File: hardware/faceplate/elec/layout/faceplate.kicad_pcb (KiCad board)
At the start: 2 copper layers, 182.9 x 128.5 mm, 65 parts

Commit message: wip
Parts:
- moved ENC64 7.00 mm to (12.6, 83.4)
- moved ENC65 7.00 mm to (107.3, 83.4)
- moved J10 7.00 mm to (170.6, 50.0)
- moved J11 7.00 mm to (128.6, 64.0)
- moved J12 7.00 mm to (142.6, 64.0)
- moved J13 7.00 mm to (156.6, 64.0)
- moved J14 7.00 mm to (170.6, 64.0)
- moved J15 7.00 mm to (128.6, 76.4)
- moved J16 7.00 mm to (142.6, 76.4)
- moved J17 7.00 mm to (156.6, 76.4)
- moved J18 7.00 mm to (170.6, 76.4)
- moved J19 7.00 mm to (128.6, 88.8)
- moved J20 7.00 mm to (142.6, 88.8)
- moved J21 7.00 mm to (156.6, 88.8)
- moved J22 7.00 mm to (170.6, 88.8)
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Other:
- board size 182.9 x 128.5 mm -> 181.9 x 127.5 mm

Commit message: Routed
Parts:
- moved J23 8.52 mm to (124.0, 94.0)
- moved J19 8.18 mm to (124.0, 82.0)
- moved J24 8.03 mm to (139.0, 94.0)
- moved J15 7.85 mm to (124.0, 70.0)
- moved J20 7.67 mm to (139.0, 82.0)
- moved J25 7.64 mm to (154.0, 94.0)
- moved J11 7.53 mm to (124.0, 58.0)
- moved J26 7.36 mm to (169.0, 94.0)
- moved J16 7.32 mm to (139.0, 70.0)
- moved J21 7.26 mm to (154.0, 82.0)
- moved J27 7.22 mm to (124.0, 108.0)
- moved J22 6.97 mm to (169.0, 82.0)
- moved J12 6.97 mm to (139.0, 58.0)
- moved J17 6.89 mm to (154.0, 70.0)
- moved J28 6.63 mm to (139.0, 108.0)
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
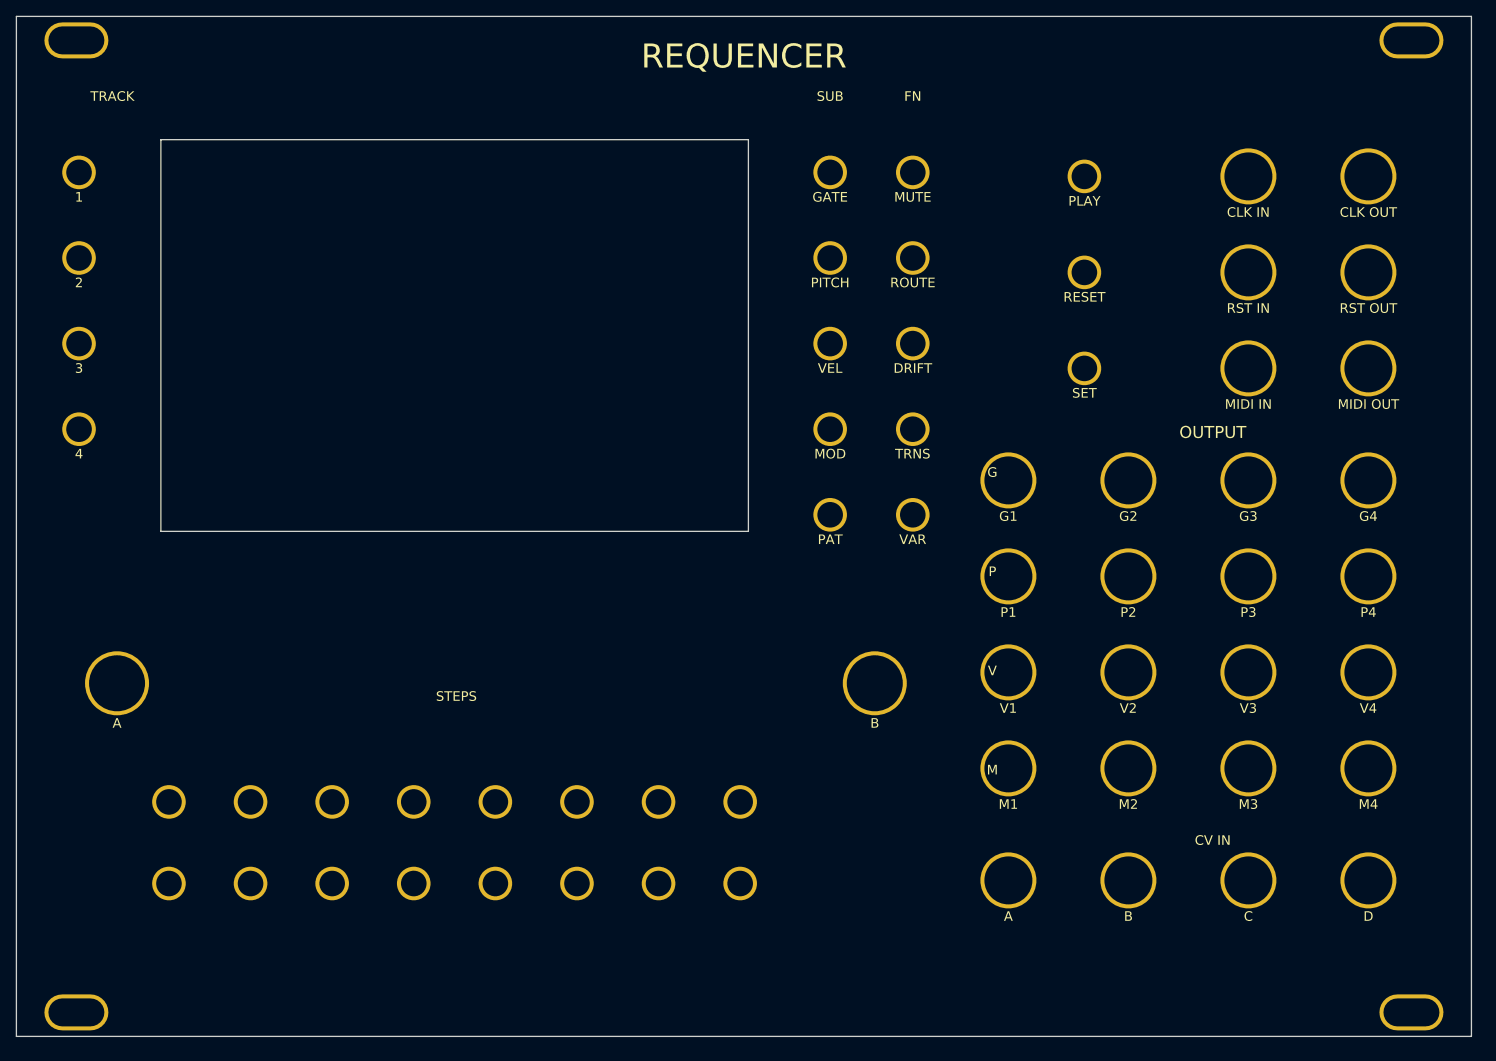
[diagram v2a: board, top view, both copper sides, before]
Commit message: Fix hardware pipeline: SD card position, faceplate holes, 3D assembly stack-up
- Fix SD card slot placement below PLAY button with component-map fallback
- Rebuild PJS008U 3D model as hollow card cage, align with faceplate cutout
- Inset USB-C connector flush with main board edge
- Add clock jack holes, SD cutout, JetBrains Mono fonts to faceplate
- Correct 3D assembly Z spacing from actual PJ398SM model measurements
- Improve explode animation: anchor control board, smoother slider
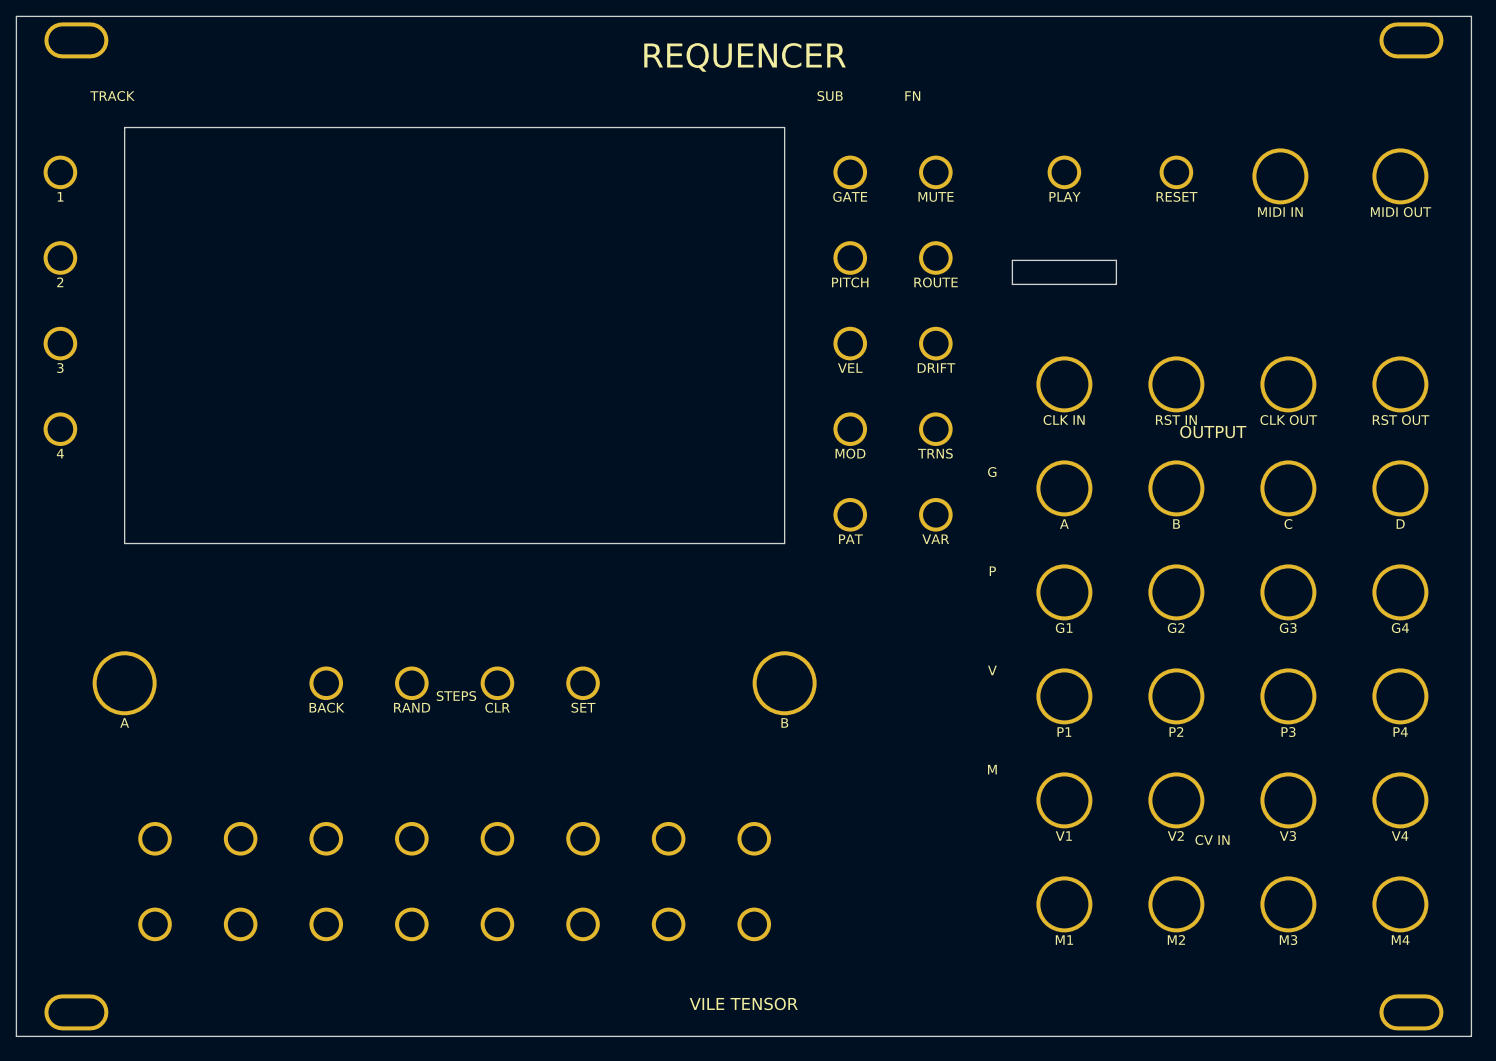
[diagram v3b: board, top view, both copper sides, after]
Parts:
- removed ENC64: , Faceplate:ENC64
- removed ENC65: , Faceplate:ENC65
- added ENC67: , Faceplate:ENC67, F.Cu at (13.5, 83.4)
- added ENC68: , Faceplate:ENC68, F.Cu at (96.0, 83.4)
- added SW64: , Faceplate:SW64, F.Cu at (49.4, 83.4)
- added SW65: , Faceplate:SW65, F.Cu at (60.1, 83.4)
- added SW66: , Faceplate:SW66, F.Cu at (104.2, 62.3)
- moved SW62 74.0 mm to (70.8, 83.4)
- moved SW63 66.4 mm to (38.7, 83.4)
- moved J27 49.5 mm to (131.0, 59.0)
- moved J28 49.4 mm to (145.0, 59.0)
- moved J29 49.3 mm to (159.0, 59.0)
- moved J30 49.2 mm to (173.0, 59.0)
- moved J7 26.9 mm to (131.0, 46.0)
- moved J23 18.4 mm to (131.0, 111.0)
- moved J24 18.0 mm to (145.0, 111.0)
- moved J25 17.7 mm to (159.0, 111.0)
- moved J19 17.5 mm to (131.0, 98.0)
- moved J26 17.5 mm to (173.0, 111.0)
- moved J8 17.2 mm to (159.0, 46.0)
- moved J20 17.1 mm to (145.0, 98.0)
- moved SW61 17.0 mm to (145.0, 19.5)
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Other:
- outline, holes or cut-outs redrawn
- board text added: "VILE TENSOR"

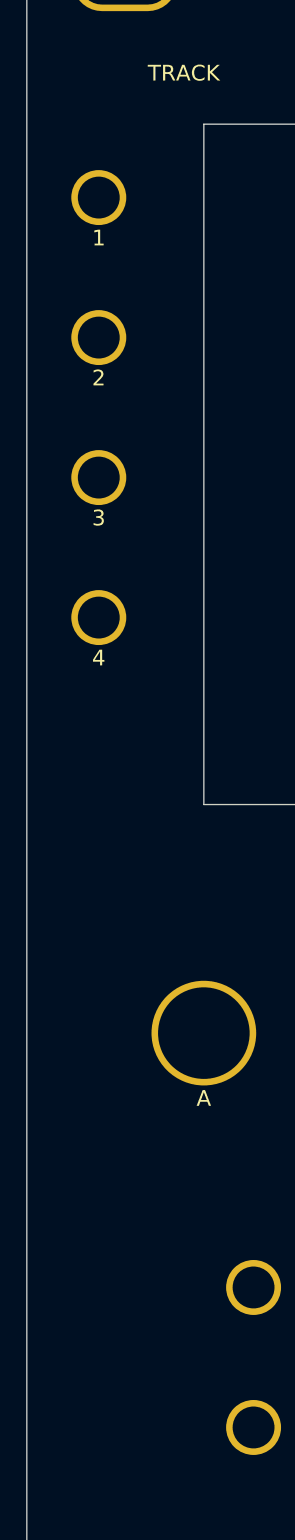
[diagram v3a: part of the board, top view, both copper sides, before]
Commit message: Throughhole m3 for stability
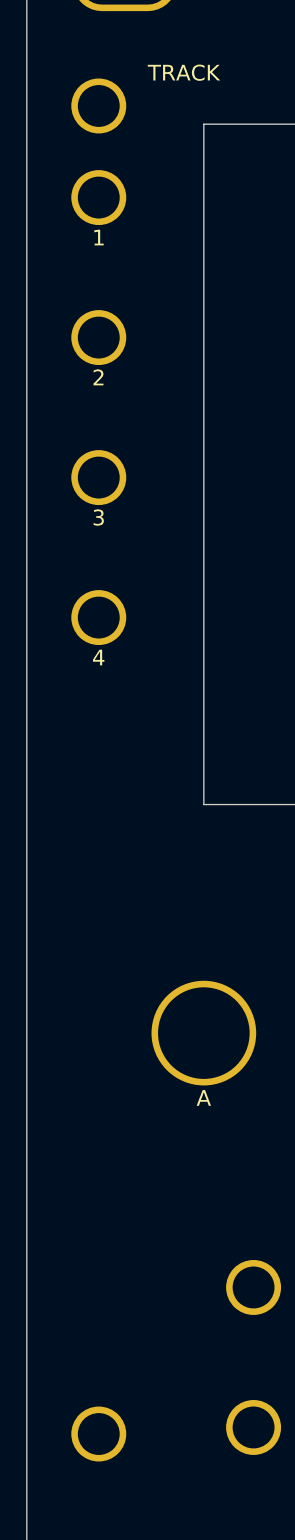
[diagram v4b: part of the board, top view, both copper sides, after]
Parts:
- removed ENC67: , Faceplate:ENC67
- removed ENC68: , Faceplate:ENC68
- removed J5: , Faceplate:J5
- removed J6: , Faceplate:J6
- removed SW31: , Faceplate:SW31
- removed SW32: , Faceplate:SW32
- added ENC69: , Faceplate:ENC69, F.Cu at (13.5, 83.4)
- added ENC70: , Faceplate:ENC70, F.Cu at (96.0, 83.4)
- added J31: , Faceplate:J31, F.Cu at (159.0, 59.0)
- added J32: , Faceplate:J32, F.Cu at (173.0, 59.0)
- added SO5: , Faceplate:SO5, F.Cu at (5.50, 12.5)
- added SO6: , Faceplate:SO6, F.Cu at (5.50, 114.0)
- added SW67: , Faceplate:SW67, F.Cu at (60.1, 83.4)
- added SW68: , Faceplate:SW68, F.Cu at (104.2, 62.3)
- moved SW63 124.0 mm to (145.0, 19.5)
- moved SW44 110.2 mm to (114.9, 51.6)
- moved SW61 107.8 mm to (92.2, 113.5)
- moved SW60 106.2 mm to (81.5, 113.5)
- moved SW35 101.0 mm to (5.50, 40.9)
- moved SW36 101.0 mm to (5.50, 51.6)
- moved SW45 95.9 mm to (114.9, 62.3)
- moved SW62 87.7 mm to (131.0, 19.5)
- moved SW52 65.1 mm to (81.5, 102.8)
- moved SW53 65.1 mm to (92.2, 102.8)
- moved J27 59.1 mm to (159.0, 111.0)
- moved J28 59.1 mm to (173.0, 111.0)
- moved SW66 58.7 mm to (49.4, 83.4)
- moved J12 38.2 mm to (173.0, 46.0)
- moved J7 37.5 mm to (158.0, 20.0)
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
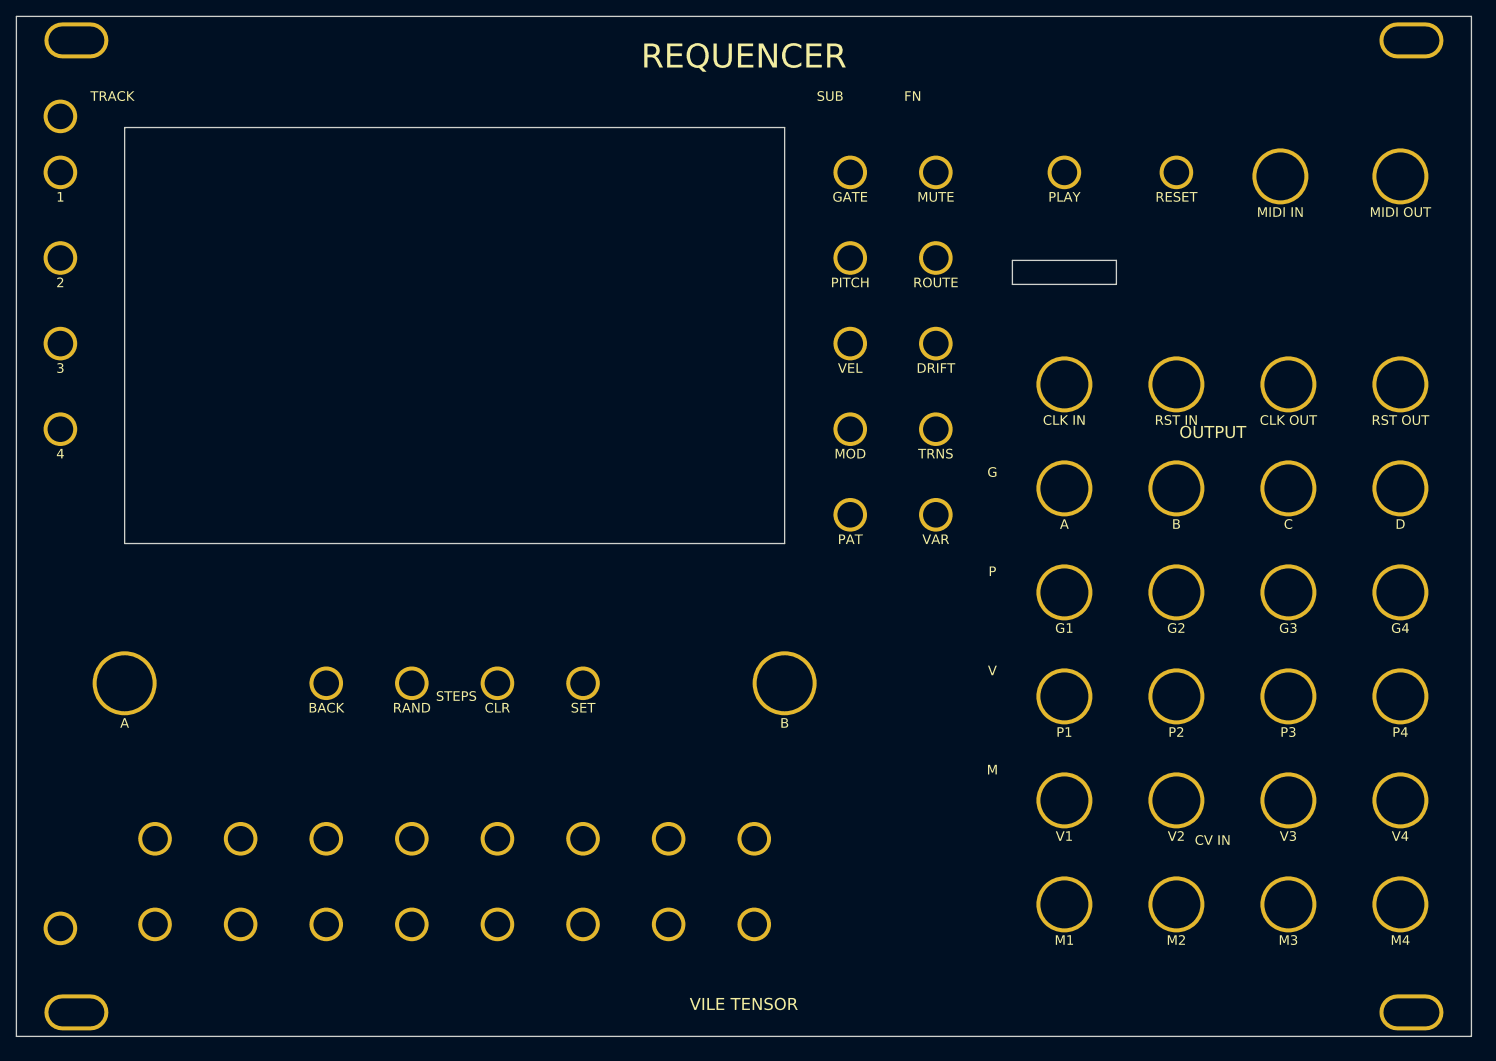
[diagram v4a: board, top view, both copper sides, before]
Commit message: Refactor hardware pipeline: config-driven scripts, immutable build stages, full 3D export
- Reorganize scripts/ into build/, common/, placement/, routing/, export/, models/
- Replace autoroute.sh (389 lines bash) with autoroute.py (pure Python)
- Extract board-specific values into board-config.json (placement, routing, DRC allowlist)
- Create hardware/Makefile with file-based dependencies covering full pipeline
- Immutable pipeline: placed → routed → poured → 3d → step → glb (no in-place mutation)
- Ground pours now read clearances from design-rules.json
- DRC allowlisting for known SD card footprint errors
- 3D pipeline: add_3d_models → export_3d_assembly (STEP) → export_gltf (GLB with named nodes)
- Simplify root Makefile to delegate hw-* targets to hardware/Makefile
- Remove Docker/CI workflows (unused), old flat scripts, pycache
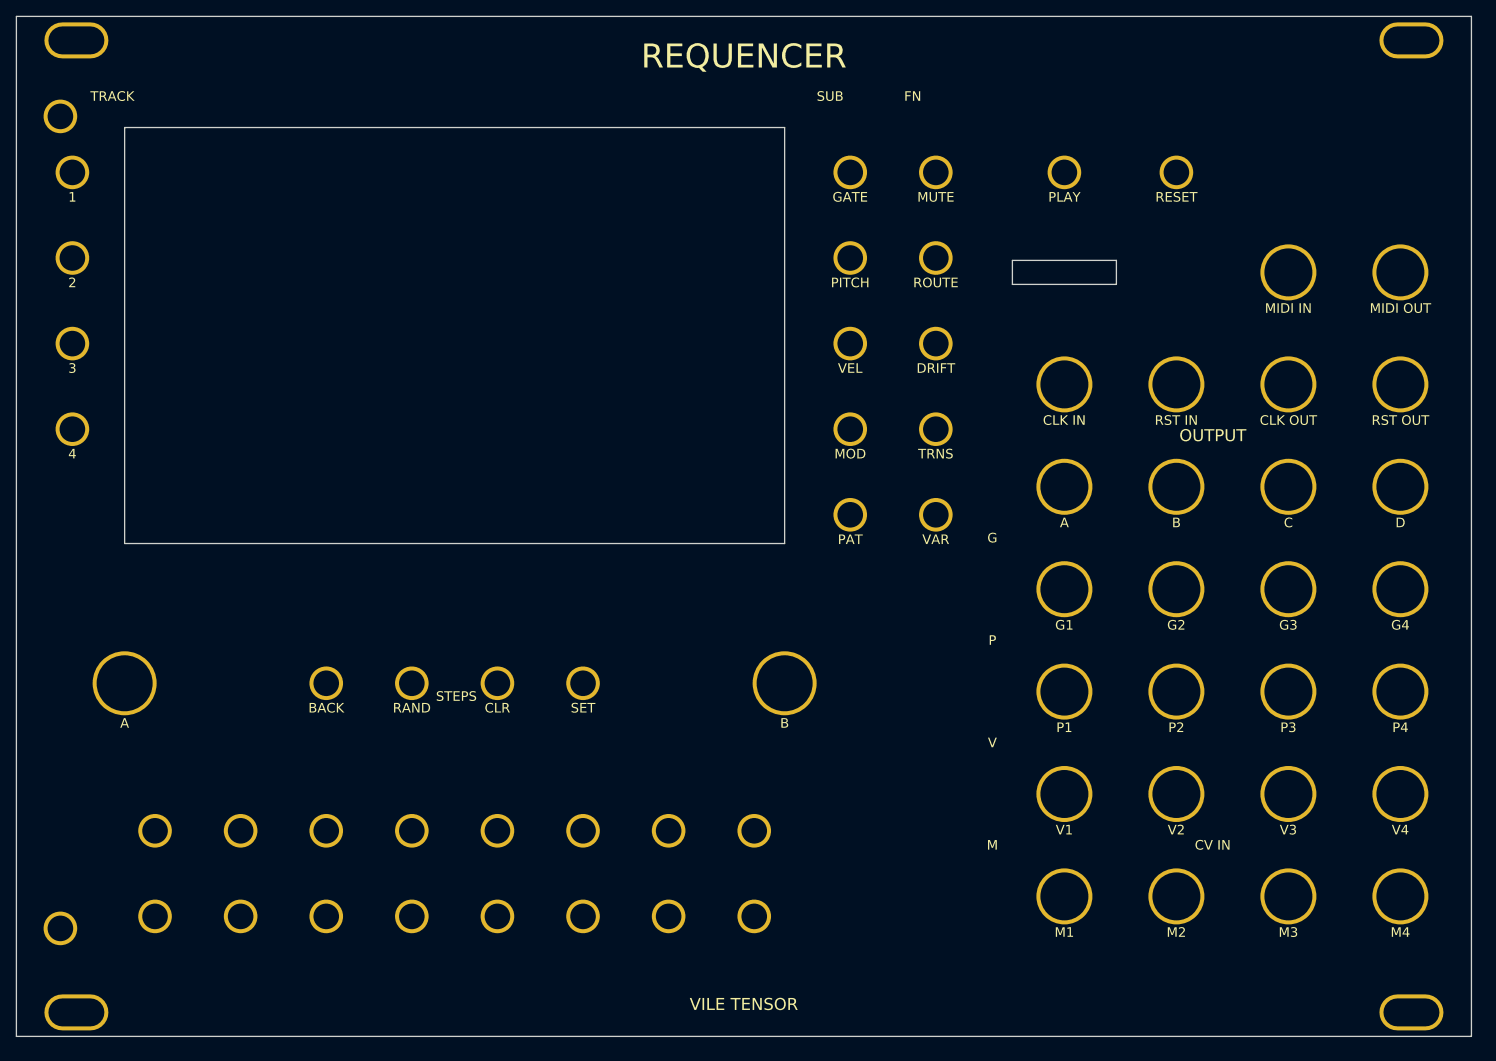
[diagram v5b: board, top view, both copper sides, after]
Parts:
- moved J7 12.0 mm to (159.0, 32.0)
- moved J8 12.0 mm to (173.0, 32.0)
- moved SW33 1.50 mm to (7.00, 19.5)
- moved SW34 1.50 mm to (7.00, 30.2)
- moved SW35 1.50 mm to (7.00, 40.9)
- moved SW36 1.50 mm to (7.00, 51.6)
- moved J25 1.00 mm to (131.0, 110.0)
- moved J26 1.00 mm to (145.0, 110.0)
- moved J27 1.00 mm to (159.0, 110.0)
- moved J28 1.00 mm to (173.0, 110.0)
- moved SW46 1.00 mm to (17.3, 101.8)
- moved SW47 1.00 mm to (28.0, 101.8)
- moved SW48 1.00 mm to (38.7, 101.8)
- moved SW49 1.00 mm to (49.4, 101.8)
- moved SW50 1.00 mm to (60.1, 101.8)
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
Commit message: Multi algo
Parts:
- moved J8 89.1 mm to (130.9, 110.5)
- moved J7 69.1 mm to (130.9, 95.1)
- moved J9 16.6 mm to (141.9, 33.5)
- moved J11 14.8 mm to (152.9, 33.5)
- moved J29 14.7 mm to (141.9, 48.9)
- moved J10 13.4 mm to (163.9, 33.5)
- moved J13 13.1 mm to (141.9, 64.3)
- moved J30 12.7 mm to (152.9, 48.9)
- moved J12 12.6 mm to (174.9, 33.5)
- moved J17 11.9 mm to (141.9, 79.7)
- moved J21 11.1 mm to (141.9, 95.1)
- moved J31 11.0 mm to (163.9, 48.9)
- moved J25 10.9 mm to (141.9, 110.5)
- moved J14 10.8 mm to (152.9, 64.3)
- moved J32 10.1 mm to (174.9, 48.9)
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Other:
- outline, holes or cut-outs redrawn
- board text added: "C"
- board text added: "E"
- board text added: "N"
- board text added: "Q"
- board text added: "R"
- board text added: "U"
- board text removed: "CV IN"
- board text removed: "FN"
- board text removed: "G"
- board text removed: "M"
- board text removed: "OUTPUT"
- board text removed: "P"
- board text removed: "REQUENCER"
- board text removed: "STEPS"
- board text removed: "SUB"
- board text removed: "TRACK"
- board text removed: "V"
